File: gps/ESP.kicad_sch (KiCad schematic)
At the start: 9 parts, among them J10 Conn_01x02, J11 Conn_01x02, J6 Conn_01x04, J7 USB_B_Micro, J8 Conn_01x04, SW1 RotaryEncoder_Switch, U3 DFR0654

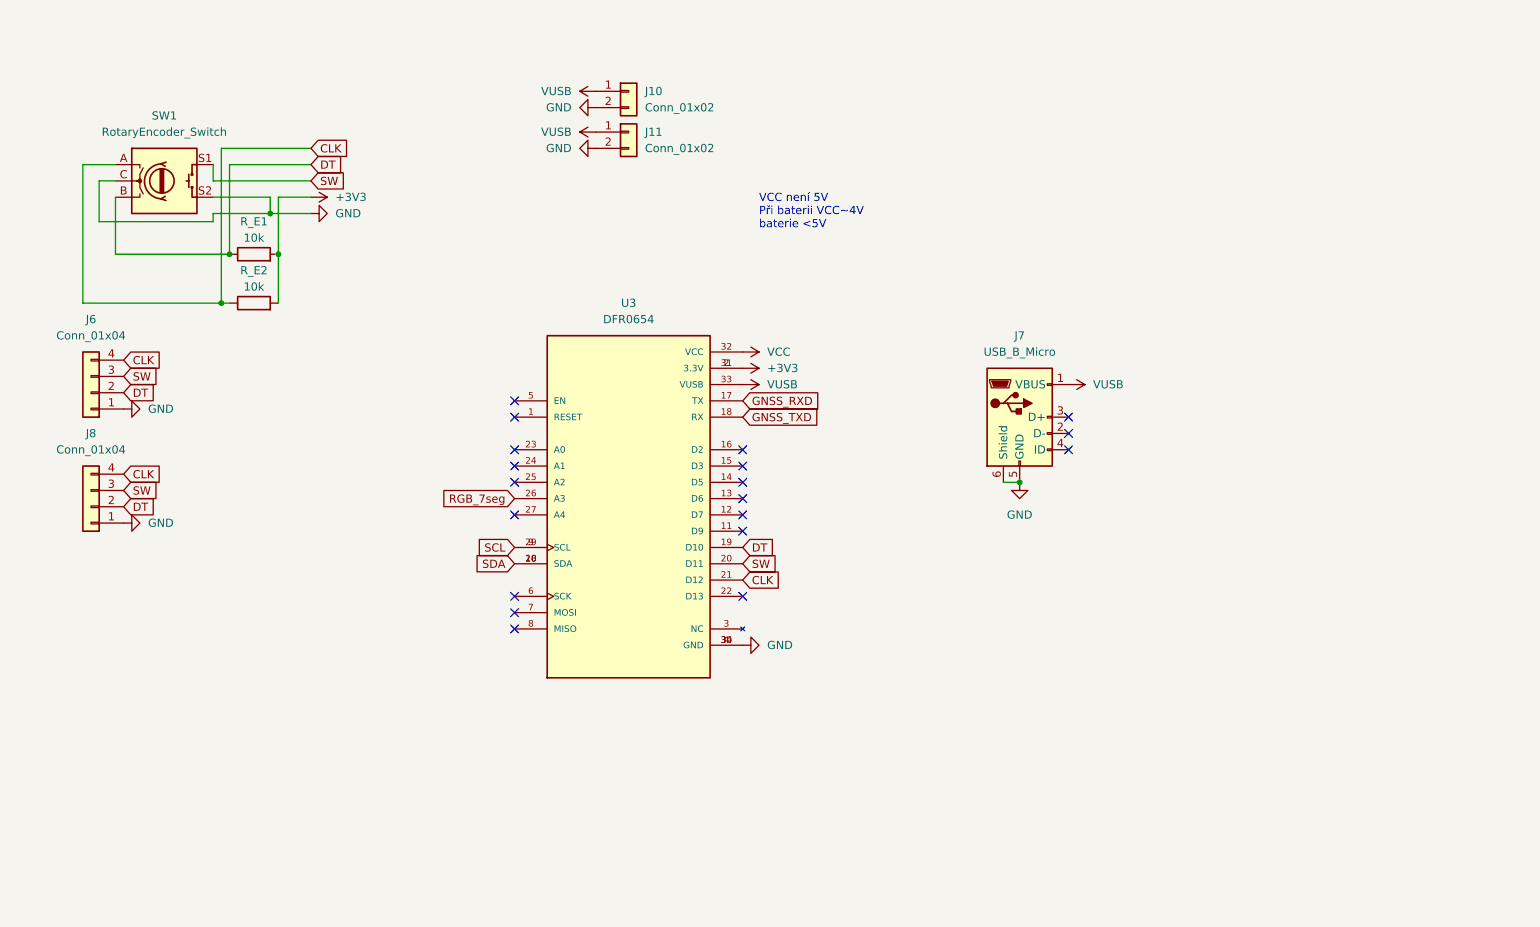
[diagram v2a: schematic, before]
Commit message: update pcb/housing
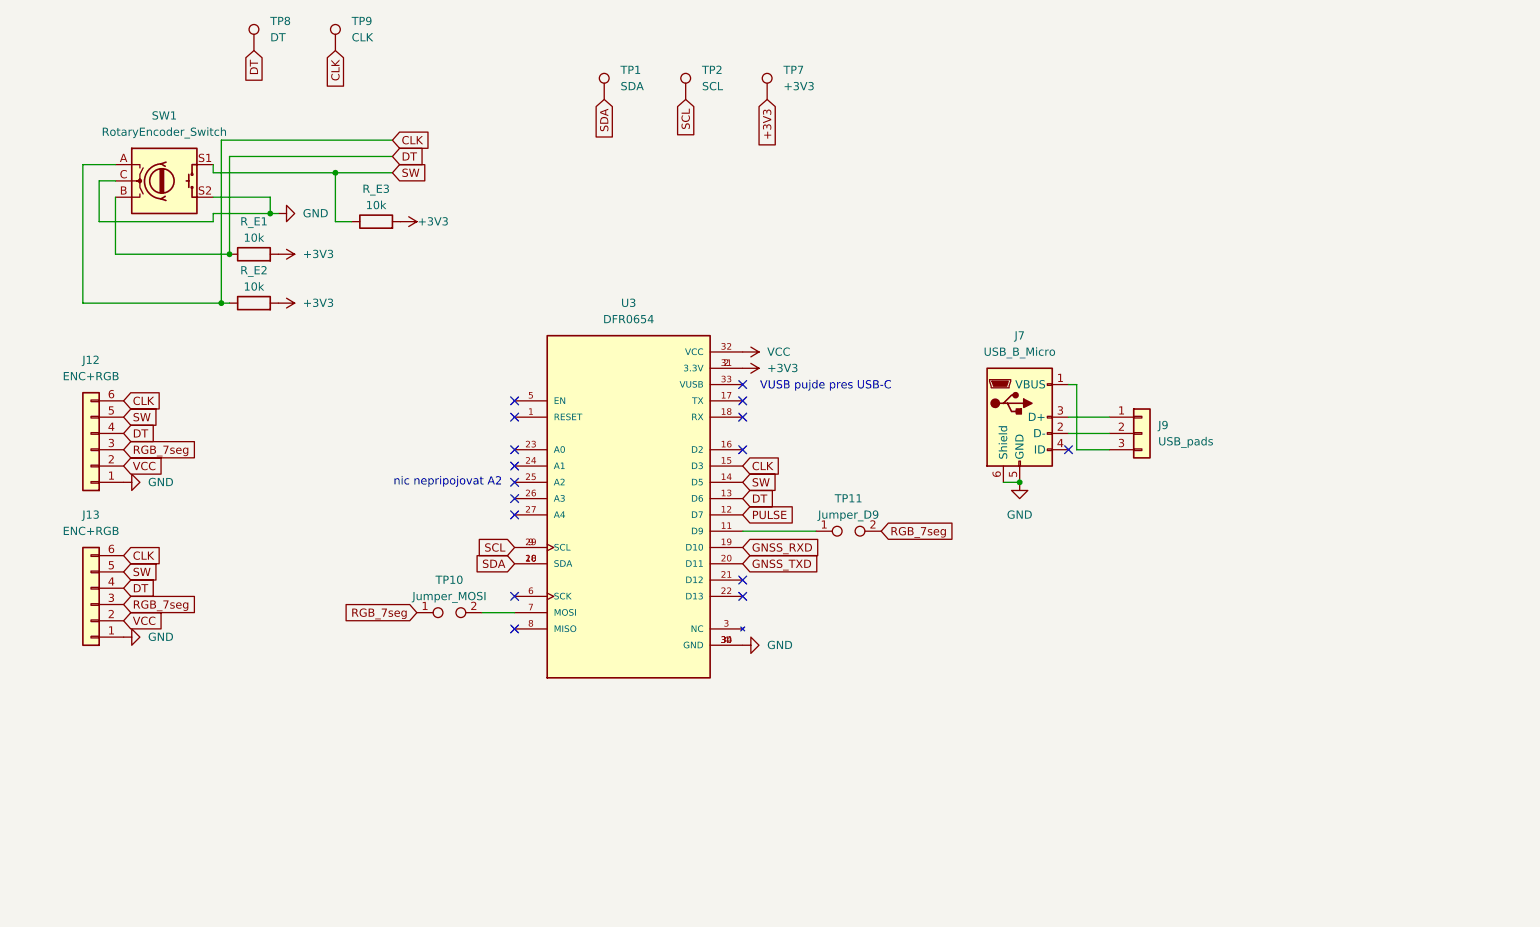
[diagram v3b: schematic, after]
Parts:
- removed J10: Conn_01x02, Connector_PinHeader_2.54mm:PinHeader_1x02_P2.54mm_Vertical, symbol Connector_Generic:Conn_01x02
- removed J11: Conn_01x02, Connector_PinSocket_2.54mm:PinSocket_1x02_P2.54mm_Vertical, symbol Connector_Generic:Conn_01x02
- removed J6: Conn_01x04, Connector_PinHeader_2.54mm:PinHeader_1x04_P2.54mm_Vertical, symbol Connector_Generic:Conn_01x04
- removed J8: Conn_01x04, Connector_PinSocket_2.54mm:PinSocket_1x04_P2.54mm_Vertical, symbol Connector_Generic:Conn_01x04
- added J12: ENC+RGB, Connector_PinSocket_2.54mm:PinSocket_1x06_P2.54mm_Vertical, symbol Connector_Generic:Conn_01x06
- added J13: ENC+RGB, Connector_PinHeader_2.54mm:PinHeader_1x06_P2.54mm_Vertical, symbol Connector_Generic:Conn_01x06
- added J9: USB_pads, Connector_PinSocket_2.54mm:PinSocket_1x03_P2.54mm_Vertical, symbol Connector_Generic:Conn_01x03
- added R_E3: 10k, Resistor_SMD:R_0603_1608Metric_Pad0.98x0.95mm_HandSolder, symbol Device:R
- added TP1: SDA, TestPoint:TestPoint_Loop_D1.80mm_Drill1.0mm_Beaded, symbol Connector:TestPoint
- added TP10: Jumper_MOSI, Jumper:SolderJumper-2_P1.3mm_Bridged_RoundedPad1.0x1.5mm, symbol Connector:TestPoint_2Pole
- added TP11: Jumper_D9, Jumper:SolderJumper-2_P1.3mm_Bridged_RoundedPad1.0x1.5mm, symbol Connector:TestPoint_2Pole
- added TP2: SCL, TestPoint:TestPoint_Loop_D1.80mm_Drill1.0mm_Beaded, symbol Connector:TestPoint
- added TP7: +3V3, TestPoint:TestPoint_Loop_D1.80mm_Drill1.0mm_Beaded, symbol Connector:TestPoint
- added TP8: DT, TestPoint:TestPoint_Loop_D1.80mm_Drill1.0mm_Beaded, symbol Connector:TestPoint
- added TP9: CLK, TestPoint:TestPoint_Loop_D1.80mm_Drill1.0mm_Beaded, symbol Connector:TestPoint
- U3: footprint DFR0654:MODULE_DFR0654 -> DFR0654:DFR0654_2
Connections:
- net +3V3: now also R_E3.2, TP7.1
- net CLK: now also U3.15 (D3), J12.6 (Pin_6), J13.6 (Pin_6), TP9.1; no longer U3.21 (D12)
- net DT: now also U3.13 (D6), J12.4 (Pin_4), J13.4 (Pin_4), TP8.1; no longer U3.19 (D10)
- net GND: now also J12.1 (Pin_1), J13.1 (Pin_1)
- net GNSS_RXD: now also U3.19 (D10); no longer U3.17 (TX)
- net GNSS_TXD: now also U3.20 (D11); no longer U3.18 (RX)
- net RGB_7seg: now also J12.3 (Pin_3), J13.3 (Pin_3), TP10.1, TP11.2; no longer U3.26 (A3)
- net SCL: now also TP2.1
- net SDA: now also TP1.1
- net SW: now also U3.14 (D5), J12.5 (Pin_5), J13.5 (Pin_5), R_E3.1; no longer U3.20 (D11)
- net VCC: now also J12.2 (Pin_2), J13.2 (Pin_2)
- net at J7.2 (D-): now also J9.2 (Pin_2)
- net at J7.3 (D+): now also J9.1 (Pin_1)
- net at U3.11 (D9): now also TP11.1
- net PULSE: now reaches U3.12 (D7)
- net at U3.7 (MOSI): now also TP10.2
- net VUSB: no longer names the net of J7.1 (VBUS)
- net VUSB: now also J9.3 (Pin_3); no longer U3.33 (VUSB)
- no-connect marks 19 -> 16
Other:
- note added: "VUSB pujde pres USB-C"
- note added: "nic nepripojovat A2"
- note removed: "VCC není 5V Při baterii VCC~4V baterie <5V"

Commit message: update
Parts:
- added TP12: IO22, TestPoint:TestPoint_Loop_D1.80mm_Drill1.0mm_Beaded, symbol Connector:TestPoint
- added TP13: IO21, TestPoint:TestPoint_Loop_D1.80mm_Drill1.0mm_Beaded, symbol Connector:TestPoint
- R_E1, R_E2, R_E3: footprint Resistor_SMD:R_0603_1608Metric_Pad0.98x0.95mm_HandSolder -> Resistor_SMD:R_0805_2012Metric_Pad1.20x1.40mm_HandSolder
- TP10, TP11: footprint Jumper:SolderJumper-2_P1.3mm_Bridged_RoundedPad1.0x1.5mm -> Resistor_SMD:R_0805_2012Metric_Pad1.20x1.40mm_HandSolder
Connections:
- net CLK: now also U3.16 (D2); no longer U3.15 (D3)
- net DT: now also U3.27 (A4); no longer U3.13 (D6)
- net PULSE: now also U3.13 (D6); no longer U3.12 (D7)
- net SW: now also U3.15 (D3); no longer U3.14 (D5)
- net at TP11.1: now also U3.12 (D7); no longer U3.11 (D9)
- net at U3.21 (D12): now also TP13.1
- net at U3.22 (D13): now also TP12.1
- no-connect marks 16 -> 14
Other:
- note added: "D5 zaroven na tlačiku desky"
- note added: "D9 pin na LED desky"
- moved on the sheet: TP11

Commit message: PCB-update
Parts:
- SW1: footprint Rotary_Encoder:RotaryEncoder_Alps_EC12E-Switch_Vertical_H20mm_CircularMountingHoles -> Rotary_Encoder:RotaryEncoder_20mm_WO_mount_holes
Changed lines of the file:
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@@
 			)
 		)
-		(property "Footprint" "Rotary_Encoder:RotaryEncoder_Alps_EC12E-Switch_Vertical_H20mm_CircularMountingHoles"
+		(property "Footprint" "Rotary_Encoder:RotaryEncoder_20mm_WO_mount_holes"
 			(at 44.45 41.656 0)
 			(effects

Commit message: tweaks
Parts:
- J7: footprint Connector_USB:USB_Mini-B_Tensility_54-00023_Vertical_CircularHoles -> KiCad:USB3145301A
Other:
- moved on the sheet: R_E1, R_E2, R_E3

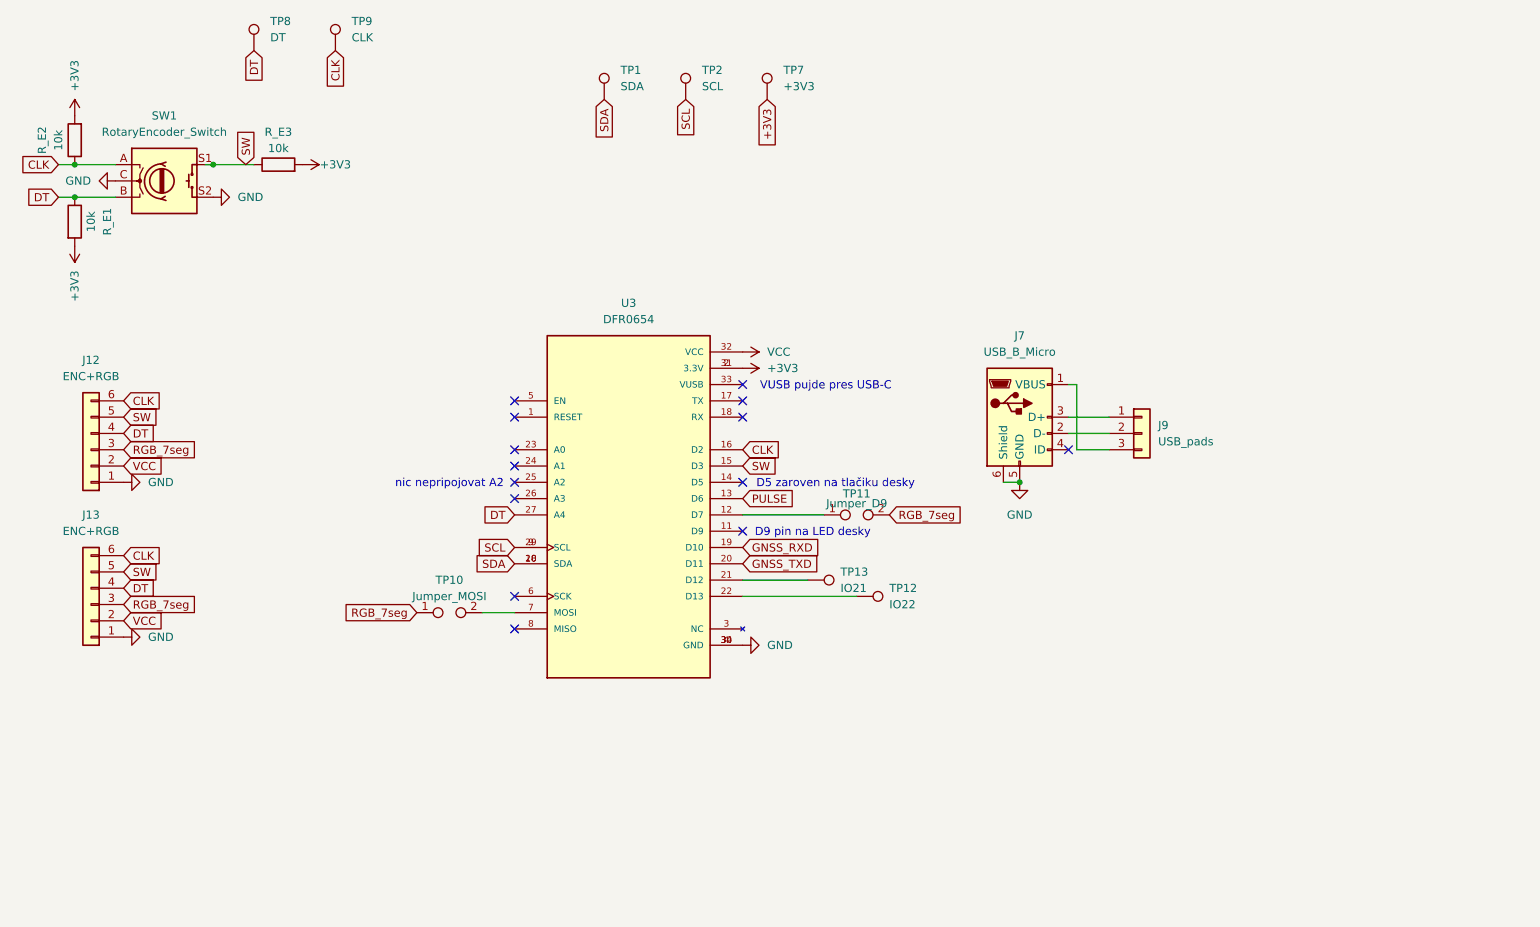
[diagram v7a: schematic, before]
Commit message: added level shifters for i2C and RGB displey,
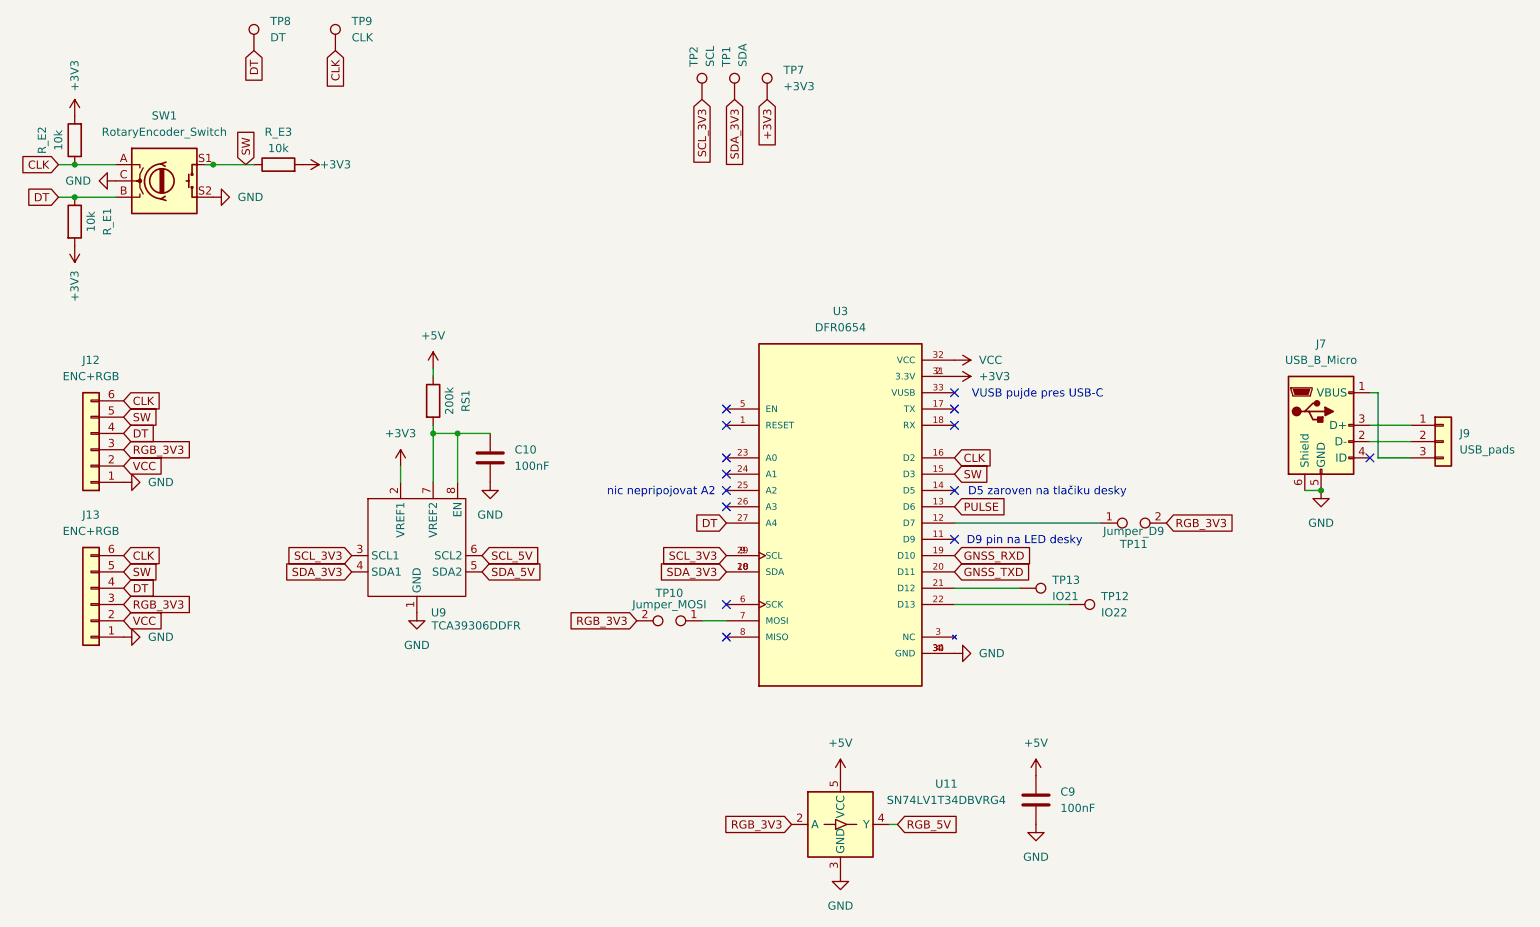
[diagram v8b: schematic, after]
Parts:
- added C10, C9: 100nF, Capacitor_SMD:C_0805_2012Metric_Pad1.18x1.45mm_HandSolder, symbol Device:C
- added RS1: 200k, Resistor_SMD:R_0805_2012Metric_Pad1.20x1.40mm_HandSolder, symbol Device:R
- added U11: SN74LV1T34DBVRG4, Package_TO_SOT_SMD:SOT-23-5, symbol Logic_LevelTranslator:SN74LV1T34DBV
- added U9: TCA39306DDFR, Package_TO_SOT_SMD:SOT-23-8, symbol shifter:TCA39306DCURQ1
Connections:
- net +3V3: now also U9.2 (VREF1)
- net GND: now also C10.1, C9.1, U11.3 (GND), U9.1 (GND)
- net at U3.7 (MOSI): now also TP10.1; no longer TP10.2
- net RGB_7seg renamed RGB_3V3
- net RGB_3V3: now also TP10.2, U11.2 (A); no longer TP10.1
- net SCL renamed SCL_3V3
- net SCL_3V3: now also U9.3 (SCL1)
- net SDA renamed SDA_3V3
- net SDA_3V3: now also U9.4 (SDA1)
- new net: C10.2, RS1.2, U9.7 (VREF2), U9.8 (EN)
- new net +5V: C9.2, RS1.1, U11.5 (VCC)
- new net RGB_5V: U11.4 (Y)
- new net SCL_5V: U9.6 (SCL2)
- new net SDA_5V: U9.5 (SDA2)
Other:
- moved on the sheet: J7, J9, TP1, TP10, TP11, TP12, TP13, TP2, U3
